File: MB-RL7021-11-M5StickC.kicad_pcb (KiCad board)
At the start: 2 copper layers, 65 x 20 mm, 7 parts, among them J1 Conn_01x08, U1 MB-RL7021-11

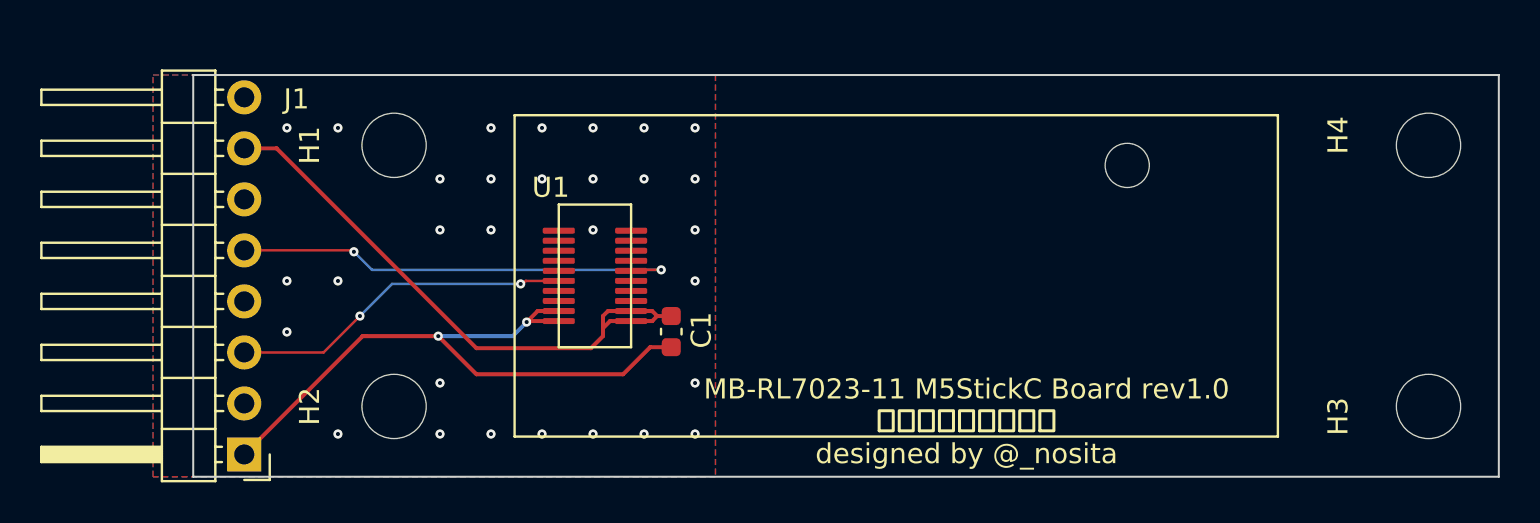
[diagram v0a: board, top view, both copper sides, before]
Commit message: ver1.1 ねじをm2に変更
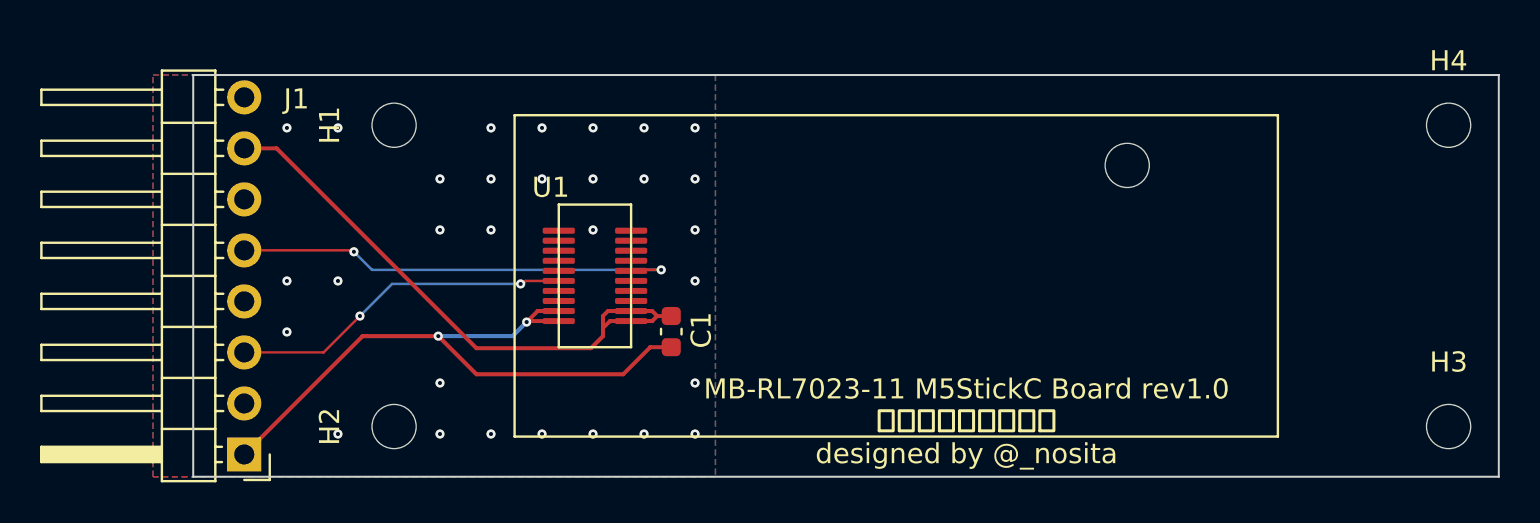
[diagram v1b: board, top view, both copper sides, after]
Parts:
- H1, H2, H3, H4: footprint MountingHole:MountingHole_3.2mm_M3 -> MountingHole:MountingHole_2.2mm_M2
- moved H3 1.41 mm to (180.5, 124.5)
- moved H4 1.41 mm to (180.5, 109.5)
- moved H1 1.00 mm to (128.0, 109.5)
- moved H2 1.00 mm to (128.0, 124.5)
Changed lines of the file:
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@@
   (net 21 "unconnected-(U1-Pad19)")
   (net 22 "unconnected-(U1-Pad20)")
-  (footprint "MountingHole:MountingHole_3.2mm_M3" (layer "F.Cu")
-    (at 128 123.5 90)
-    (descr "Mounting Hole 3.2mm, no annular, M3")
-    (tags "mounting hole 3.2mm no annular m3")
+  (footprint "MountingHole:MountingHole_2.2mm_M2" (layer "F.Cu")
+    (at 128 124.5 90)
+    (descr "Mounting Hole 2.2mm, no annular, M2")
+    (tags "mounting hole 2.2mm no annular m2")
     (property "Sheetfile" "MB-RL7021-11-M5StickC.kicad_sch")
     (property "Sheetname" "")
     (attr exclude_from_pos_files)
-    (fp_text reference "H2" (at 0 -4.2 90) (layer "F.SilkS")
-      (effects (font (size 1 1) (thickness 0.15)))
-    )
-    (fp_text value "MountingHole" (at -4.625 2.09 180) (layer "F.Fab")
+    (fp_text reference "H2" (at 0 -3.2 90) (layer "F.SilkS")
+      (effects (font (size 1 1) (thickness 0.15)))
+    )
+    (fp_text value "MountingHole" (at 0 3.2 90) (layer "F.Fab")
       (effects (font (size 1 1) (thickness 0.15)))
     )
@@
       (effects (font (size 1 1) (thickness 0.15)))
     )
-    (fp_circle (center 0 0) (end 3.2 0) (layer "Cmts.User") (width 0.15) (fill none))
-    (fp_circle (center 0 0) (end 3.45 0) (layer "F.CrtYd") (width 0.05) (fill none))
-    (pad "" np_thru_hole circle (at 0 0 90) (size 3.2 3.2) (drill 3.2) (layers *.Cu *.Mask))
-  )
-  (footprint "MountingHole:MountingHole_3.2mm_M3" (layer "F.Cu")
-    (at 179.5 110.5)
-    (descr "Mounting Hole 3.2mm, no annular, M3")
-    (tags "mounting hole 3.2mm no annular m3")
+    (fp_circle (center 0 0) (end 2.2 0) (layer "Cmts.User") (width 0.15) (fill none))
+    (fp_circle (center 0 0) (end 2.45 0) (layer "F.CrtYd") (width 0.05) (fill none))
+    (pad "" np_thru_hole circle (at 0 0 90) (size 2.2 2.2) (drill 2.2) (layers *.Cu *.Mask))
+  )
+  (footprint "MountingHole:MountingHole_2.2mm_M2" (layer "F.Cu")
+    (at 180.5 109.5)
+    (descr "Mounting Hole 2.2mm, no annular, M2")
+    (tags "mounting hole 2.2mm no annular m2")
     (property "Sheetfile" "MB-RL7021-11-M5StickC.kicad_sch")
     (property "Sheetname" "")
     (attr exclude_from_pos_files)
-    (fp_text reference "H4" (at -4.5 -0.5 90) (layer "F.SilkS")
-      (effects (font (size 1 1) (thickness 0.15)))
-    )
-    (fp_text value "MountingHole" (at 4.5 -0.5 90) (layer "F.Fab")
+    (fp_text reference "H4" (at 0 -3.2) (layer "F.SilkS")
+      (effects (font (size 1 1) (thickness 0.15)))
+    )
+    (fp_text value "MountingHole" (at 0 3.2) (layer "F.Fab")
       (effects (font (size 1 1) (thickness 0.15)))
     )
@@
       (effects (font (size 1 1) (thickness 0.15)))
     )
-    (fp_circle (center 0 0) (end 3.2 0) (layer "Cmts.User") (width 0.15) (fill none))
-    (fp_circle (center 0 0) (end 3.45 0) (layer "F.CrtYd") (width 0.05) (fill none))
-    (pad "" np_thru_hole circle (at 0 0) (size 3.2 3.2) (drill 3.2) (layers *.Cu *.Mask))
+    (fp_circle (center 0 0) (end 2.2 0) (layer "Cmts.User") (width 0.15) (fill none))
+    (fp_circle (center 0 0) (end 2.45 0) (layer "F.CrtYd") (width 0.05) (fill none))
+    (pad "" np_thru_hole circle (at 0 0) (size 2.2 2.2) (drill 2.2) (layers *.Cu *.Mask))
   )
   (footprint "taki:MB-RL7021-11" (layer "F.Cu")
@@
     )
   )
-  (footprint "MountingHole:MountingHole_3.2mm_M3" (layer "F.Cu")
-    (at 128 110.5 90)
-    (descr "Mounting Hole 3.2mm, no annular, M3")
-    (tags "mounting hole 3.2mm no annular m3")
+  (footprint "MountingHole:MountingHole_2.2mm_M2" (layer "F.Cu")
+    (at 128 109.5 90)
+    (descr "Mounting Hole 2.2mm, no annular, M2")
+    (tags "mounting hole 2.2mm no annular m2")
     (property "Sheetfile" "MB-RL7021-11-M5StickC.kicad_sch")
     (property "Sheetname" "")
     (attr exclude_from_pos_files)
-    (fp_text reference "H1" (at 0 -4.2 90) (layer "F.SilkS")
-      (effects (font (size 1 1) (thickness 0.15)))
-    )
-    (fp_text value "MountingHole" (at 4.6 0.6 180) (layer "F.Fab")
+    (fp_text reference "H1" (at 0 -3.2 90) (layer "F.SilkS")
+      (effects (font (size 1 1) (thickness 0.15)))
+    )
+    (fp_text value "MountingHole" (at 0 3.2 90) (layer "F.Fab")
       (effects (font (size 1 1) (thickness 0.15)))
     )
@@
       (effects (font (size 1 1) (thickness 0.15)))
     )
-    (fp_circle (center 0 0) (end 3.2 0) (layer "Cmts.User") (width 0.15) (fill none))
-    (fp_circle (center 0 0) (end 3.45 0) (layer "F.CrtYd") (width 0.05) (fill none))
-    (pad "" np_thru_hole circle (at 0 0 90) (size 3.2 3.2) (drill 3.2) (layers *.Cu *.Mask))
-  )
-  (footprint "MountingHole:MountingHole_3.2mm_M3" (layer "F.Cu")
-    (at 179.5 123.5)
-    (descr "Mounting Hole 3.2mm, no annular, M3")
-    (tags "mounting hole 3.2mm no annular m3")
+    (fp_circle (center 0 0) (end 2.2 0) (layer "Cmts.User") (width 0.15) (fill none))
+    (fp_circle (center 0 0) (end 2.45 0) (layer "F.CrtYd") (width 0.05) (fill none))
+    (pad "" np_thru_hole circle (at 0 0 90) (size 2.2 2.2) (drill 2.2) (layers *.Cu *.Mask))
+  )
+  (footprint "MountingHole:MountingHole_2.2mm_M2" (layer "F.Cu")
+    (at 180.5 124.5)
+    (descr "Mounting Hole 2.2mm, no annular, M2")
+    (tags "mounting hole 2.2mm no annular m2")
     (property "Sheetfile" "MB-RL7021-11-M5StickC.kicad_sch")
     (property "Sheetname" "")
     (attr exclude_from_pos_files)
-    (fp_text reference "H3" (at -4.5 0.5 90) (layer "F.SilkS")
-      (effects (font (size 1 1) (thickness 0.15)))
-    )
-    (fp_text value "MountingHole" (at 4.5 0.5 90) (layer "F.Fab")
+    (fp_text reference "H3" (at 0 -3.2) (layer "F.SilkS")
+      (effects (font (size 1 1) (thickness 0.15)))
+    )
+    (fp_text value "MountingHole" (at 0 3.2) (layer "F.Fab")
       (effects (font (size 1 1) (thickness 0.15)))
     )
@@
       (effects (font (size 1 1) (thickness 0.15)))
     )
-    (fp_circle (center 0 0) (end 3.2 0) (layer "Cmts.User") (width 0.15) (fill none))
-    (fp_circle (center 0 0) (end 3.45 0) (layer "F.CrtYd") (width 0.05) (fill none))
-    (pad "" np_thru_hole circle (at 0 0) (size 3.2 3.2) (drill 3.2) (layers *.Cu *.Mask))
+    (fp_circle (center 0 0) (end 2.2 0) (layer "Cmts.User") (width 0.15) (fill none))
+    (fp_circle (center 0 0) (end 2.45 0) (layer "F.CrtYd") (width 0.05) (fill none))
+    (pad "" np_thru_hole circle (at 0 0) (size 2.2 2.2) (drill 2.2) (layers *.Cu *.Mask))
   )
   (gr_line (start 183 107) (end 118 107) (layer "Edge.Cuts") (width 0.1))
